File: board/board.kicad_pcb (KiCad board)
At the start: 2 copper layers, 191.5 x 96 mm, 52 parts, among them U1 Seeed Studio XIAO SAMD21

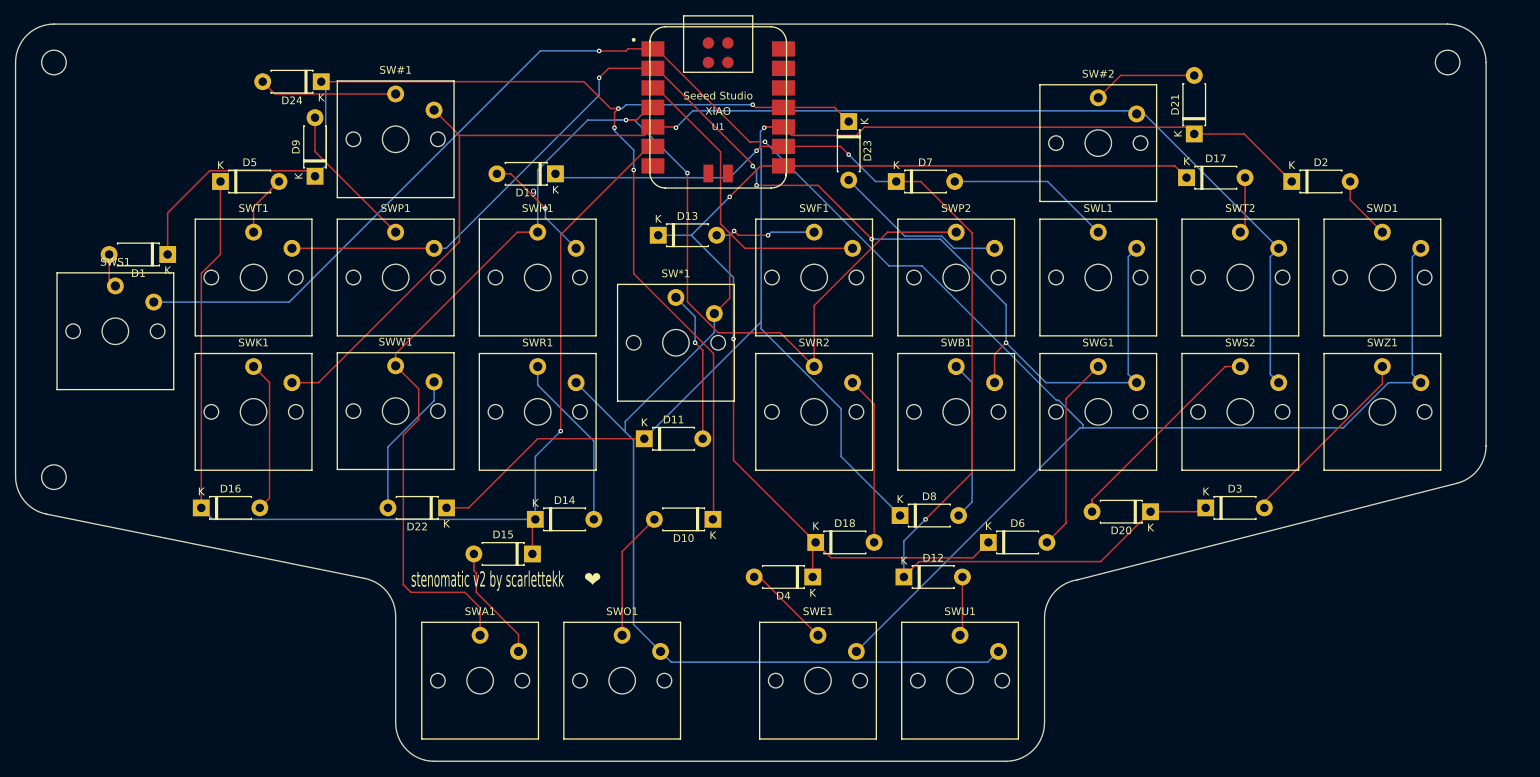
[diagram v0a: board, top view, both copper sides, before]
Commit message: add another mounting hole
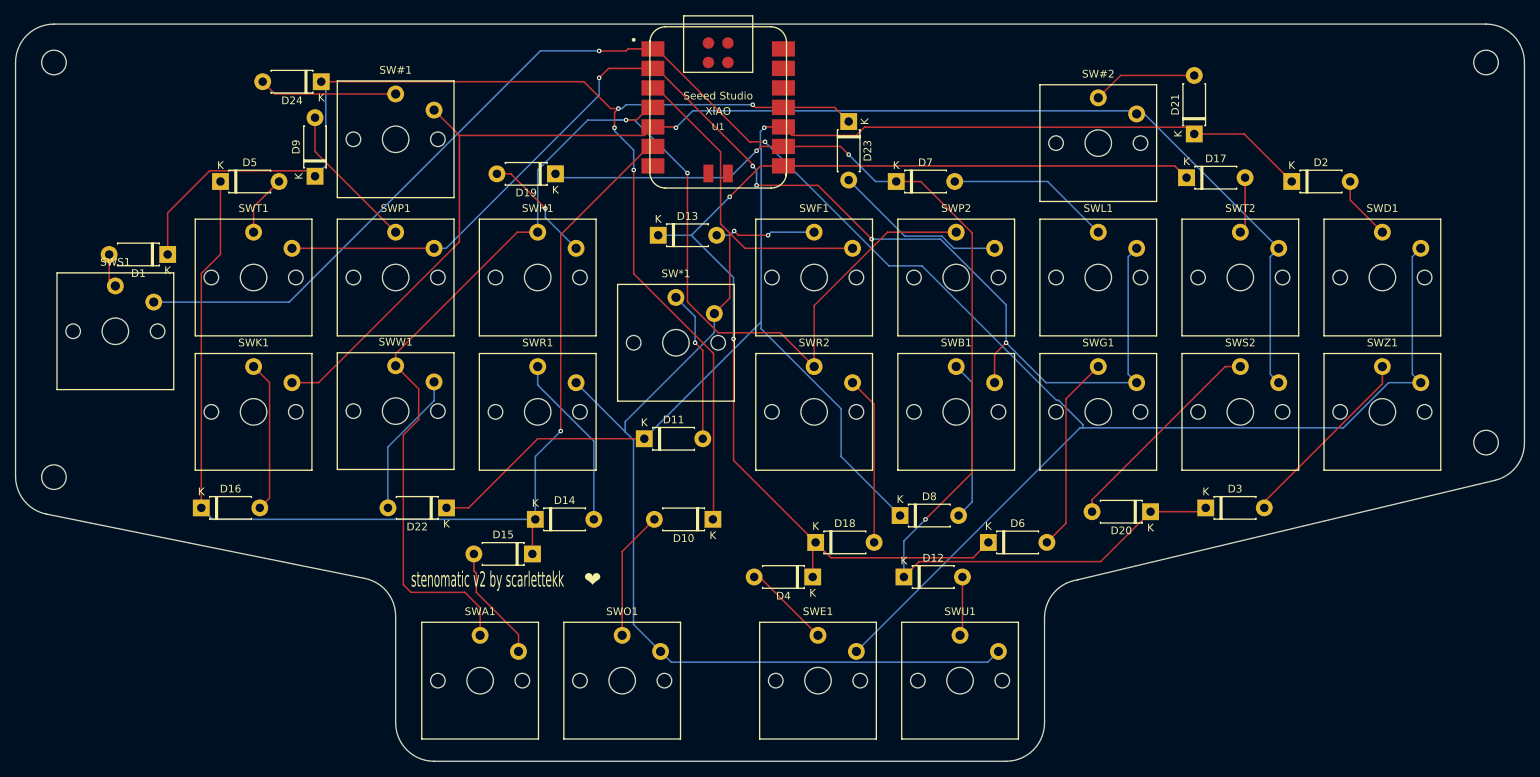
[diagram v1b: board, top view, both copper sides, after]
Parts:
- added REF**: MountingHole_3.2mm_M3, MountingHole:MountingHole_3.2mm_M3, F.Cu at (229.0, 87.5)
- moved REF** 5.00 mm to (229.0, 38.0)
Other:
- board size 191.5 x 96 mm -> 196.5 x 96 mm
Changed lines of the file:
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@@
 	(footprint "MountingHole:MountingHole_3.2mm_M3"
 		(layer "F.Cu")
-		(at 224 38)
+		(at 229 38)
 		(descr "Mounting Hole 3.2mm, no annular, M3")
 		(tags "mounting hole 3.2mm no annular m3")
@@
 		)
 	)
+	(footprint "MountingHole:MountingHole_3.2mm_M3"
+		(layer "F.Cu")
+		(at 229 87.5)
+		(descr "Mounting Hole 3.2mm, no annular, M3")
+		(tags "mounting hole 3.2mm no annular m3")
+		(property "Reference" "REF**"
+			(at 0 -4.2 0)
+			(layer "F.SilkS")
+			(hide yes)
+			(effects
+				(font
+					(size 1 1)
+					(thickness 0.15)
+				)
+			)
+		)
+		(property "Value" "MountingHole_3.2mm_M3"
+			(at 0 4.2 0)
+			(layer "F.Fab")
+			(effects
+				(font
+					(size 1 1)
+					(thickness 0.15)
+				)
+			)
+		)
+		(property "Footprint" "MountingHole:MountingHole_3.2mm_M3"
+			(at 0 0 0)
+			(unlocked yes)
+			(layer "F.Fab")
+			(hide yes)
+			(effects
+				(font
+					(size 1.27 1.27)
+					(thickness 0.15)
+				)
+			)
+		)
+		(property "Datasheet" ""
+			(at 0 0 0)
+			(unlocked yes)
+			(layer "F.Fab")
+			(hide yes)
+			(effects
+				(font
+					(size 1.27 1.27)
+					(thickness 0.15)
+				)
+			)
+		)
+		(property "Description" ""
+			(at 0 0 0)
+			(unlocked yes)
+			(layer "F.Fab")
+			(hide yes)
+			(effects
+				(font
+					(size 1.27 1.27)
+					(thickness 0.15)
+				)
+			)
+		)
+		(attr exclude_from_pos_files exclude_from_bom)
+		(fp_circle
+			(center 0 0)
+			(end 3.2 0)
+			(stroke
+				(width 0.15)
+				(type solid)
+			)
+			(fill none)
+			(layer "Cmts.User")
+		)
+		(fp_circle
+			(center 0 0)
+			(end 3.45 0)
+			(stroke
+				(width 0.05)
+				(type solid)
+			)
+			(fill none)
+			(layer "F.CrtYd")
+		)
+		(fp_text user "${REFERENCE}"
+			(at 0 0 0)
+			(layer "F.Fab")
+			(effects
+				(font
+					(size 1 1)
+					(thickness 0.15)
+				)
+			)
+		)
+		(pad "" np_thru_hole circle
+			(at 0 0)
+			(size 3.2 3.2)
+			(drill 3.2)
+			(layers "*.Cu" "*.Mask")
+		)
+	)
 	(footprint "Switch_Keyboard_Kailh:SW_Kailh_Choc_V1_1.00u"
 		(layer "F.Cu")
@@
 		(layer "Edge.Cuts")
 	)
-	(gr_line
-		(start 82.990099 105.189919)
-		(end 41.509901 96.810081)
-		(stroke
-			(width 0.05)
-			(type default)
-		)
-		(layer "Edge.Cuts")
-	)
 	(gr_arc
-		(start 224 33)
-		(mid 227.535534 34.464466)
-		(end 229 38)
+		(start 234 87.551899)
+		(mid 232.924134 90.650475)
+		(end 230.159531 92.415589)
 		(stroke
 			(width 0.05)
@@
 		(layer "Edge.Cuts")
 	)
-	(gr_arc
-		(start 229 87.949268)
-		(mid 227.947509 91.018009)
-		(end 225.233132 92.794821)
+	(gr_line
+		(start 82.990099 105.189919)
+		(end 41.509901 96.810081)
 		(stroke
 			(width 0.05)
@@
 	(gr_line
 		(start 175.782855 105.379296)
-		(end 225.233132 92.794821)
+		(end 230.159531 92.415589)
 		(stroke
 			(width 0.05)
@@
 	(gr_line
 		(start 42.5 33)
-		(end 224 33)
+		(end 229 33)
+		(stroke
+			(width 0.05)
+			(type default)
+		)
+		(layer "Edge.Cuts")
+	)
+	(gr_arc
+		(start 229 33)
+		(mid 232.535534 34.464466)
+		(end 234 38)
 		(stroke
 			(width 0.05)
@@
 	)
 	(gr_line
-		(start 229 38)
-		(end 229 87.949268)
+		(start 234 38)
+		(end 234 87.551899)
 		(stroke
 			(width 0.05)
